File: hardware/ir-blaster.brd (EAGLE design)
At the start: 83.8 x 59.7 mm, 8 parts, among them Q1 BC547

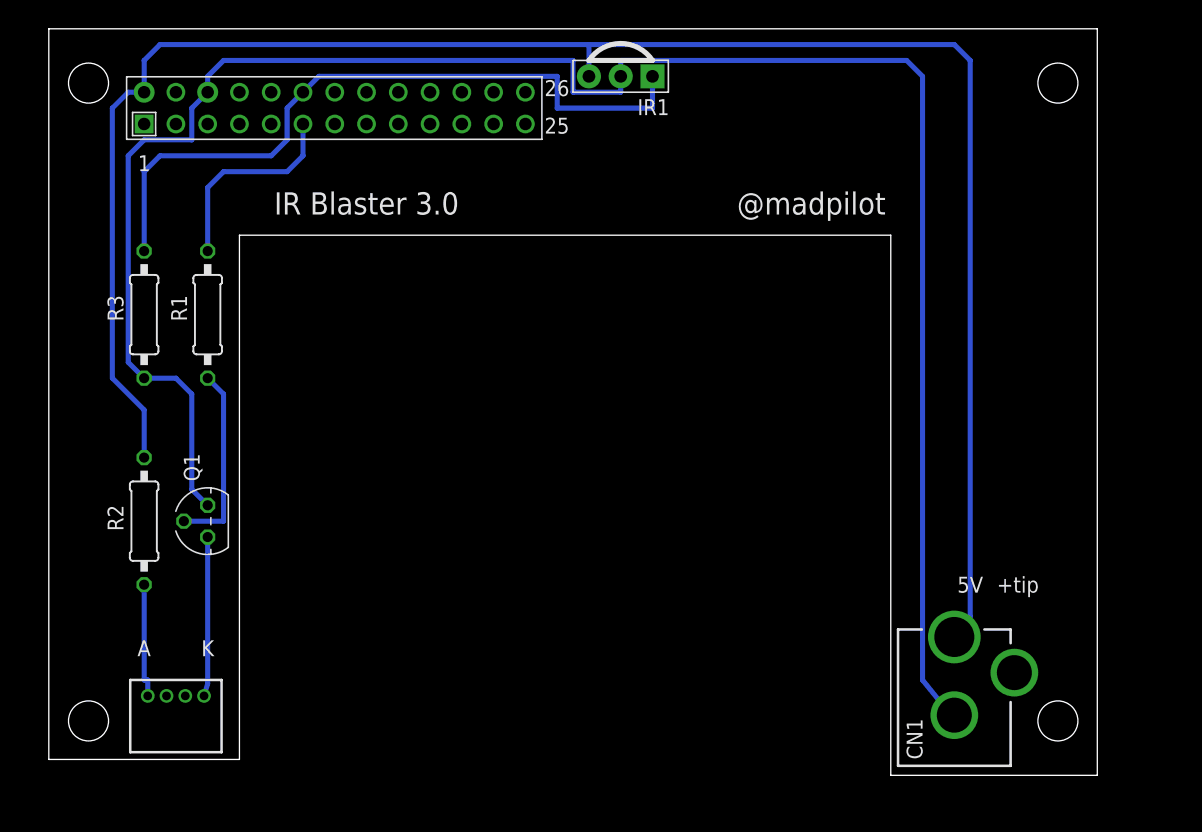
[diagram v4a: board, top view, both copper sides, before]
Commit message: Getting correct measurements for holes. Making the board cover the whole PI again. Added measurement markers for the USB WIFI dongle. Need to make up a custom pad for that
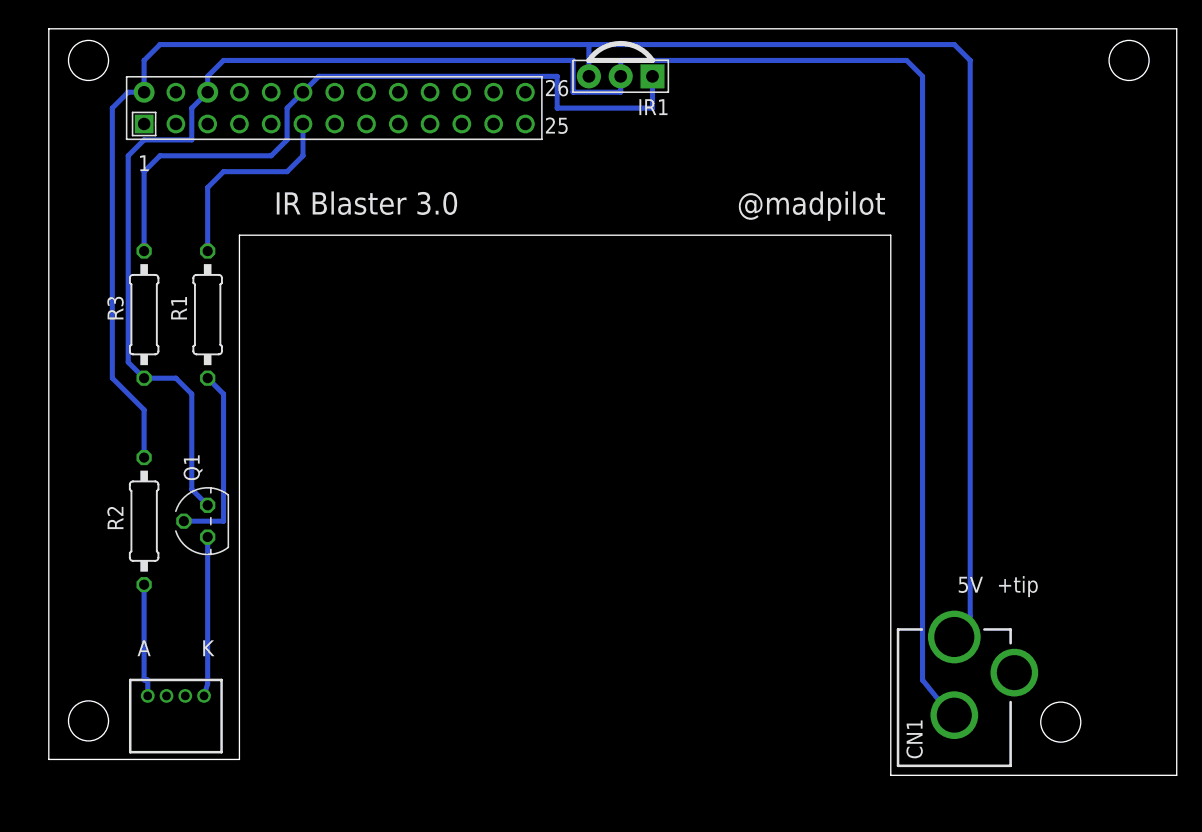
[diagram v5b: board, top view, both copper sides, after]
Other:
- board size 83.8 x 59.7 mm -> 90.2 x 59.7 mm
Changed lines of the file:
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@@
 <layer number="45" name="Holes" color="7" fill="1" visible="yes" active="yes"/>
 <layer number="46" name="Milling" color="3" fill="1" visible="no" active="yes"/>
-<layer number="47" name="Measures" color="7" fill="1" visible="no" active="yes"/>
+<layer number="47" name="Measures" color="7" fill="1" visible="yes" active="yes"/>
 <layer number="48" name="Document" color="7" fill="1" visible="no" active="yes"/>
 <layer number="49" name="Reference" color="7" fill="1" visible="no" active="yes"/>
@@
 <wire x1="10.16" y1="41.91" x2="62.23" y2="41.91" width="0" layer="20"/>
 <wire x1="62.23" y1="41.91" x2="62.23" y2="-1.27" width="0" layer="20"/>
-<wire x1="62.23" y1="-1.27" x2="78.74" y2="-1.27" width="0" layer="20"/>
-<wire x1="78.74" y1="-1.27" x2="78.74" y2="58.41" width="0" layer="20"/>
-<wire x1="78.74" y1="58.41" x2="-5.08" y2="58.41" width="0" layer="20"/>
+<wire x1="62.23" y1="-1.27" x2="85.09" y2="-1.27" width="0" layer="20"/>
+<wire x1="85.09" y1="-1.27" x2="85.09" y2="58.41" width="0" layer="20"/>
+<wire x1="85.09" y1="58.41" x2="-5.08" y2="58.41" width="0" layer="20"/>
 <wire x1="-5.08" y1="58.41" x2="-5.08" y2="0" width="0" layer="20"/>
 <text x="55.88" y="44.45" size="1.778" layer="21" font="vector" align="center">@madpilot</text>
 <text x="20.32" y="44.45" size="1.778" layer="21" font="vector" align="center">IR Blaster 3.0</text>
-<hole x="-1.905" y="54.07" drill="3.2"/>
+<hole x="-1.905" y="55.88" drill="3.2"/>
 <hole x="-1.905" y="3.08" drill="3.2"/>
-<hole x="75.58999375" y="54.07" drill="3.2"/>
+<hole x="81.28" y="55.88" drill="3.2"/>
 <text x="72.39" y="13.97" size="1.27" layer="21" font="fixed" align="center">+tip</text>
 <text x="68.58" y="13.97" size="1.27" layer="21" font="fixed" align="center">5V</text>
 <text x="2.54" y="8.89" size="1.27" layer="21" font="fixed" align="center">A</text>
 <text x="7.62" y="8.89" size="1.27" layer="21" font="fixed" align="center">K</text>
-<hole x="75.58999375" y="3.08" drill="3.2"/>
+<hole x="75.819" y="2.9845" drill="3.2"/>
+<dimension x1="85.09" y1="-7.62" x2="59.69" y2="-7.62" x3="72.39" y3="-10.16" textsize="1.778" layer="47" unit="inch"/>
+<dimension x1="92.71" y1="54.61" x2="92.71" y2="-1.27" x3="93.98" y3="26.67" textsize="1.778" layer="47" unit="inch"/>
+<dimension x1="0" y1="62.23" x2="85.09" y2="62.23" x3="42.545" y3="63.5" textsize="1.778" layer="47" unit="inch"/>
+<dimension x1="0" y1="-8.89" x2="10.16" y2="-8.89" x3="5.08" y3="-7.62" textsize="1.778" layer="47" unit="inch"/>
+<dimension x1="87.63" y1="-1.27" x2="87.63" y2="21.59" x3="88.9" y3="10.16" textsize="1.778" layer="47" unit="inch"/>
+<dimension x1="97.79" y1="21.59" x2="97.79" y2="28.448" x3="99.06" y3="25.019" textsize="1.778" layer="47" unit="inch"/>
+<dimension x1="85.09" y1="-15.24" x2="78.74" y2="-15.24" x3="81.915" y3="-15.24" textsize="1.778" layer="47" unit="inch"/>
 </plain>
 <attributes>

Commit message: Adding pads for the USB wifi dongle
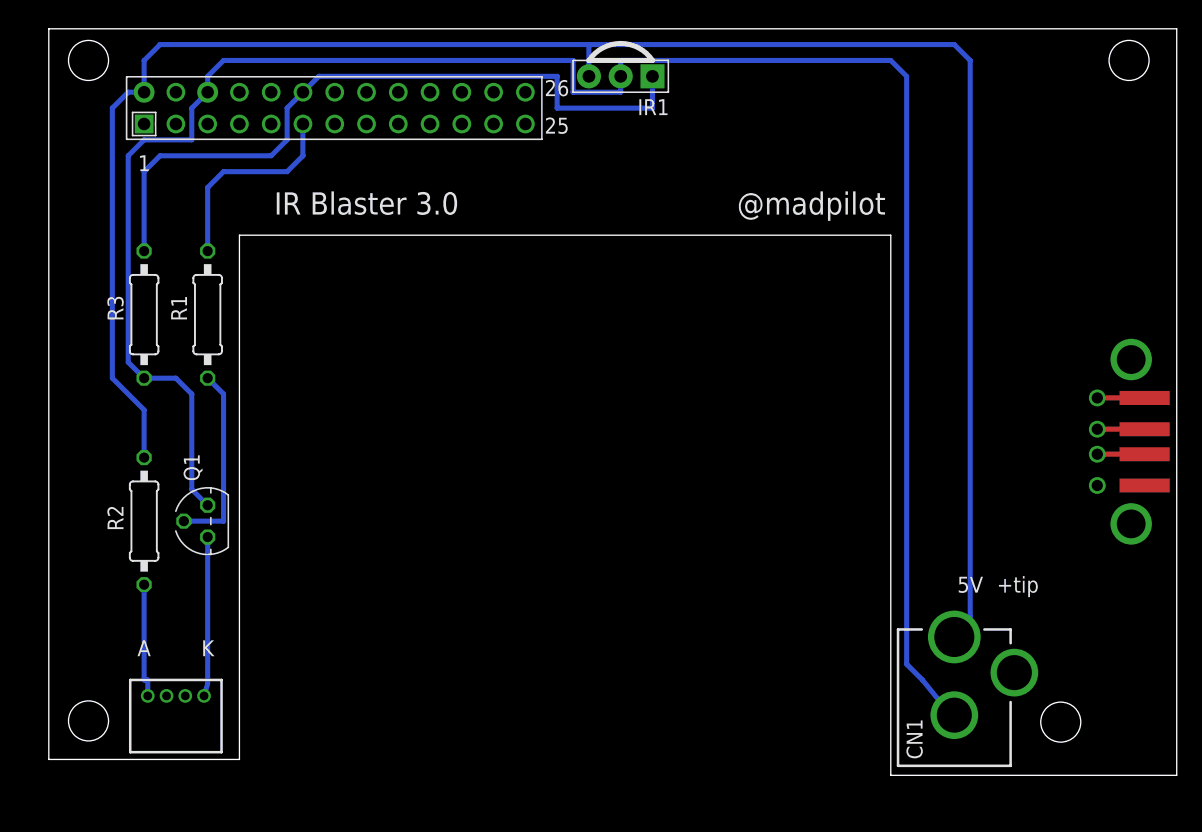
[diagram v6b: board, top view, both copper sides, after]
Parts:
- added X1: KUSBVX, con-kycon-no-mask:KUSBVX
- added X2: (no value), con-yamaichi-no-mask:USB-A003
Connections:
- new net N$3: X1.1, X2.1
- new net N$4: X1.2, X2.2
- new net N$8: X1.3, X2.3
- new net N$9: X1.4, X2.4
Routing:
- net N$9: track 0.00 -> 3.78 mm
- net N$8: track 0.00 -> 3.78 mm
- net N$4: track 0.00 -> 3.78 mm
- net GND: track 158.7 -> 158.0 mm
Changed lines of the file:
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@@
 <attribute name="VALUE" x="2.54" y="1.27" size="1.27" layer="27"/>
 </element>
+<element name="X2" library="con-yamaichi-no-mask" package="USB-A003" value="" x="83.82" y="25.4" rot="R90">
+<attribute name="MF" value="" x="83.82" y="25.4" size="1.778" layer="27" rot="R90" display="off"/>
+<attribute name="MPN" value="" x="83.82" y="25.4" size="1.778" layer="27" rot="R90" display="off"/>
+<attribute name="OC_FARNELL" value="unknown" x="83.82" y="25.4" size="1.778" layer="27" rot="R90" display="off"/>
+<attribute name="OC_NEWARK" value="unknown" x="83.82" y="25.4" size="1.778" layer="27" rot="R90" display="off"/>
+</element>
+<element name="X1" library="con-kycon-no-mask" package="KUSBVX" value="KUSBVX" x="78.74" y="25.4" rot="R270"/>
 </elements>
 <signals>
@@
 <wire x1="67.31" y1="3.54" x2="67.04" y2="3.54" width="0.4064" layer="16"/>
 <wire x1="67.04" y1="3.54" x2="64.77" y2="6.35" width="0.4064" layer="16"/>
-<wire x1="64.77" y1="6.35" x2="64.77" y2="54.61" width="0.4064" layer="16"/>
-<wire x1="64.77" y1="54.61" x2="63.5" y2="55.88" width="0.4064" layer="16"/>
-<wire x1="63.5" y1="55.88" x2="40.64" y2="55.88" width="0.4064" layer="16"/>
+<wire x1="64.77" y1="6.35" x2="63.5" y2="7.62" width="0.4064" layer="16"/>
+<wire x1="63.5" y1="7.62" x2="63.5" y2="54.61" width="0.4064" layer="16"/>
+<wire x1="63.5" y1="54.61" x2="62.23" y2="55.88" width="0.4064" layer="16"/>
+<wire x1="62.23" y1="55.88" x2="40.64" y2="55.88" width="0.4064" layer="16"/>
 </signal>
 <signal name="VCC">
@@
 <wire x1="7.62" y1="6.06" x2="7.33" y2="5.08" width="0.4064" layer="16"/>
 </signal>
+<signal name="N$3">
+<contactref element="X2" pad="1"/>
+<contactref element="X1" pad="1"/>
+<wire x1="78.74" y1="21.9" x2="82.52" y2="21.9" width="0" layer="19" extent="1-1"/>
+</signal>
+<signal name="N$4">
+<contactref element="X2" pad="2"/>
+<contactref element="X1" pad="2"/>
+<wire x1="78.74" y1="24.4" x2="82.52" y2="24.4" width="0.4064" layer="1"/>
+</signal>
+<signal name="N$8">
+<contactref element="X2" pad="3"/>
+<contactref element="X1" pad="3"/>
+<wire x1="78.74" y1="26.4" x2="82.52" y2="26.4" width="0.4064" layer="1"/>
+</signal>
+<signal name="N$9">
+<contactref element="X2" pad="4"/>
+<contactref element="X1" pad="4"/>
+<wire x1="78.74" y1="28.9" x2="82.52" y2="28.9" width="0.4064" layer="1"/>
+</signal>
 </signals>

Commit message: Working on version 3 of the board
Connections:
- net N$1: now also LED_CONN.3
- net N$2: now also LED_CONN.2
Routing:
- net N$1: track 9.18 -> 15.3 mm
- net N$2: track 12.7 -> 17.3 mm
- net N$3: track 0.00 -> 3.78 mm
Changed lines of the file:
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@@
 <contactref element="LED_CONN" pad="1"/>
 <contactref element="R2" pad="2"/>
+<contactref element="LED_CONN" pad="3"/>
 <wire x1="2.54" y1="13.97" x2="2.54" y2="6.35" width="0.4064" layer="16"/>
 <wire x1="2.54" y1="6.35" x2="2.83" y2="6.35" width="0.4064" layer="16"/>
 <wire x1="2.83" y1="6.35" x2="2.83" y2="5.08" width="0.4064" layer="16"/>
+<wire x1="2.83" y1="5.08" x2="2.54" y2="5.08" width="0.4064" layer="16"/>
+<wire x1="2.54" y1="5.08" x2="2.54" y2="3.81" width="0.4064" layer="16"/>
+<wire x1="5.83" y1="3.81" x2="5.83" y2="5.08" width="0.4064" layer="16"/>
+<wire x1="2.54" y1="3.81" x2="5.83" y2="3.81" width="0.4064" layer="16"/>
 </signal>
 <signal name="N$2">
+<contactref element="Q1" pad="3"/>
+<contactref element="LED_CONN" pad="2"/>
 <contactref element="LED_CONN" pad="4"/>
-<contactref element="Q1" pad="3"/>
-<wire x1="7.62" y1="17.78" x2="7.62" y2="6.06" width="0.4064" layer="16"/>
-<wire x1="7.62" y1="6.06" x2="7.33" y2="5.08" width="0.4064" layer="16"/>
+<wire x1="7.62" y1="17.78" x2="7.33" y2="17.78" width="0.4064" layer="16"/>
+<wire x1="7.33" y1="17.78" x2="7.33" y2="6.35" width="0.4064" layer="16"/>
+<wire x1="7.33" y1="6.35" x2="7.33" y2="5.08" width="0.4064" layer="16"/>
+<wire x1="4.33" y1="6.35" x2="4.33" y2="5.08" width="0.4064" layer="16"/>
+<wire x1="7.33" y1="6.35" x2="4.33" y2="6.35" width="0.4064" layer="16"/>
 </signal>
 <signal name="N$3">
 <contactref element="X2" pad="1"/>
 <contactref element="X1" pad="1"/>
-<wire x1="78.74" y1="21.9" x2="82.52" y2="21.9" width="0" layer="19" extent="1-1"/>
+<wire x1="78.74" y1="21.9" x2="82.52" y2="21.9" width="0.4064" layer="1"/>
 </signal>
 <signal name="N$4">
